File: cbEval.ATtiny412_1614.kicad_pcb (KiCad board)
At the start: 2 copper layers, 35 x 109 mm, 59 parts, among them J1 Bergstik-II_3, J11 Bergstik-II_3, J12 Bergstik-II_3, J13 Bergstik-II_6, J14 Bergstik-II_6, J15 Bergstik-II_6, J16 Bergstik-II_3, J17 Bergstik-II_6, J18 Bergstik-II_3, J19 Bergstik-II_6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

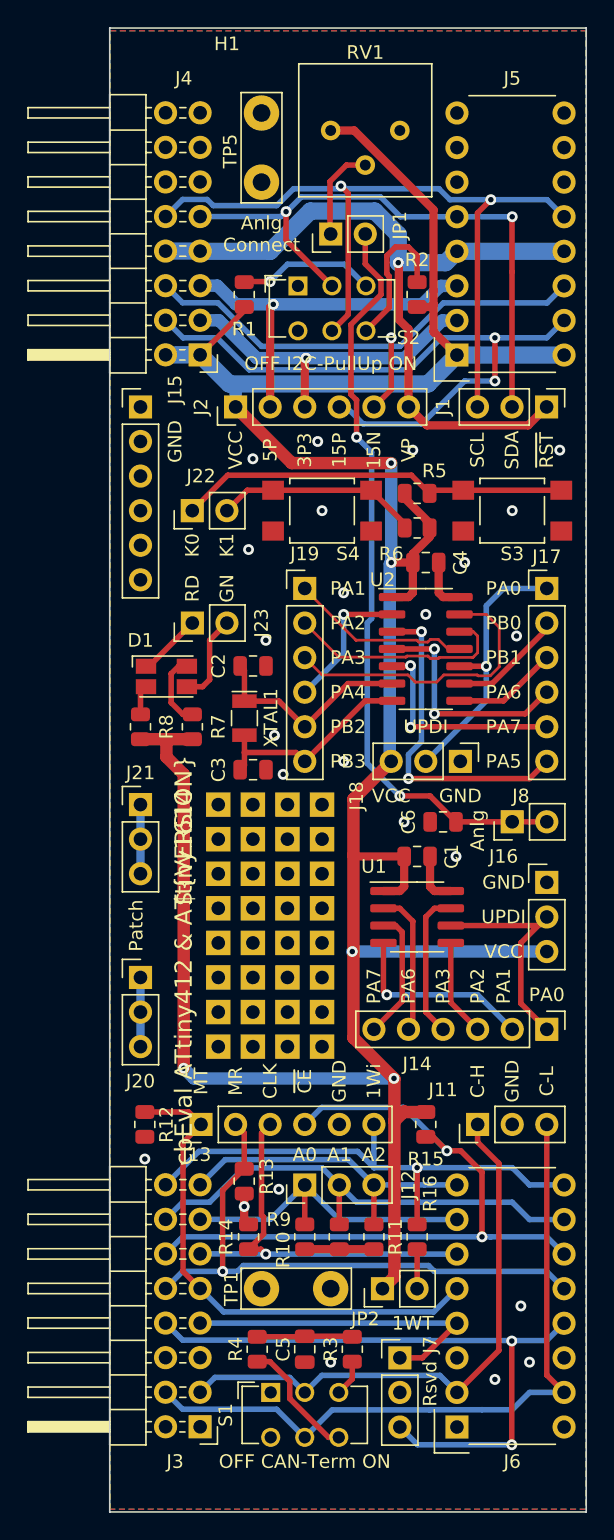
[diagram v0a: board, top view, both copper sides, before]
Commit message: Leiterplatte verkleinert, SilkScreen einiger Stecker verändert
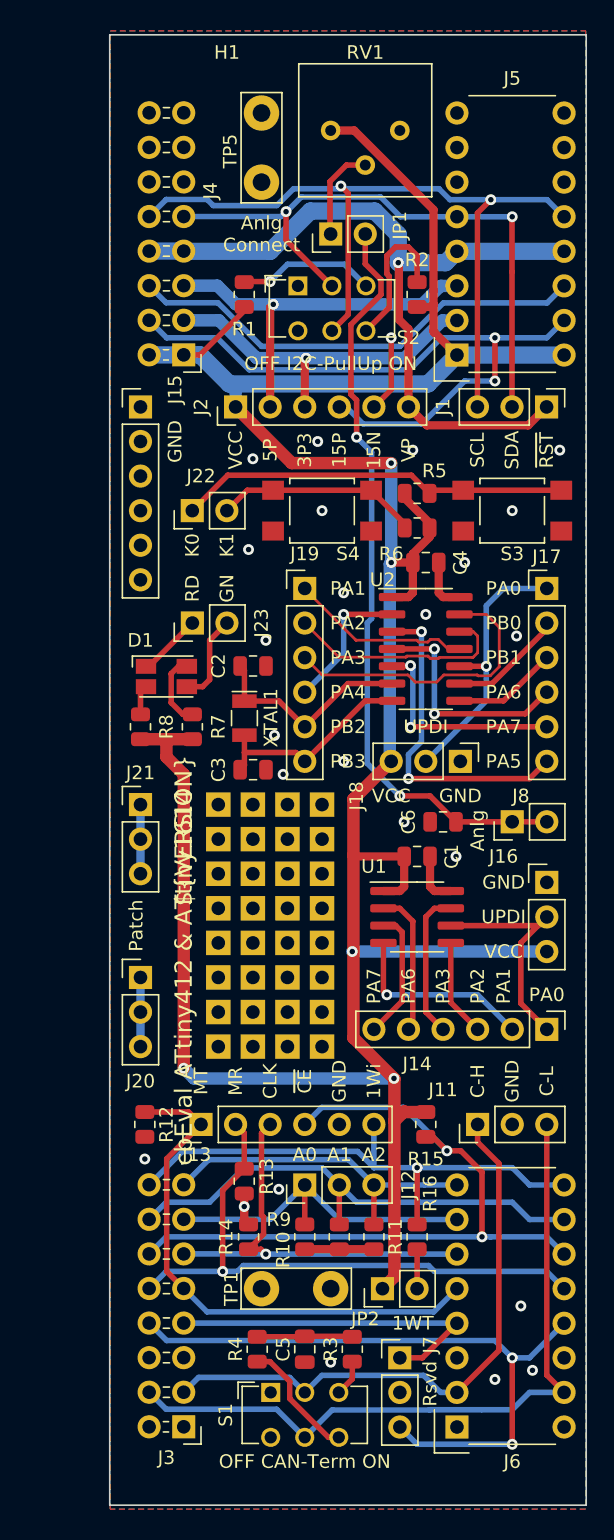
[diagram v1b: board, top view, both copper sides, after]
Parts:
- J3, J4: footprint Connector_PinHeader_2.54mm:PinHeader_2x08_P2.54mm_Horizontal -> BTech.PinHeader.2-54mm:PinHeader_2x08_P2.54mm_Horizontal
- moved J3 1.20 mm to (134.0, 149.2)
- moved J4 1.20 mm to (134.0, 70.5)
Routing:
- net VCC: track 217.7 -> 220.1 mm
- net /SPI-MTSR: track 37.9 -> 39.6 mm
- net +3V3: track 24.8 -> 26.0 mm
- net +VDC: track 55.8 -> 57.0 mm
- net /SPI-~{CE}: track 52.6 -> 53.8 mm
- net /SPI-ADR1: track 35.3 -> 36.5 mm
- net /One-Wire: track 38.7 -> 39.9 mm
- net /I2C-SCL: track 58.3 -> 59.5 mm
- net /CAN-L: track 52.2 -> 53.4 mm
- net -15V: track 39.2 -> 40.4 mm
- net /SPI-MRST: track 42.4 -> 43.6 mm
- net +15V: track 48.7 -> 49.9 mm
- net /CAN-H: track 42.4 -> 43.6 mm
- net /SPI-ADR2: track 23.3 -> 24.5 mm
- net /SPI-CLK: track 30.2 -> 31.4 mm
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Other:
- board size 35 x 109 mm -> 35 x 108 mm

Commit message: Kurzschluss entfernt, Vorwiderstand für grüne LEDs auf 560 verringert
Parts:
- R8: value 649R -> 560R
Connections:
- J1 pad 1: +VDC -> /~{RESET}
- J4 pad 8: +VDC -> /~{RESET}
- J5 pad 8: +VDC -> /~{RESET}
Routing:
- net /~{RESET}: track 0.00 -> 44.9 mm
- net +VDC: track 57.0 -> 35.3 mm
- net VCC: track 220.1 -> 221.6 mm
- net GND: vias 24 -> 25
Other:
- board text added: "V1.1.0"
- board text added: "cbEval ATtiny"
- board text removed: "${TITLE}"
- board text removed: "${VERSION}"
